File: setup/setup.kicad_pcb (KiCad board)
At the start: 2 copper layers, 54 x 94 mm, 19 parts, among them J1 Conn_01x08_Socket, J11 Motor Power, J2 Conn_01x08_Socket, J3 Step M1, J4 PS2 Controller, J5 Conn_01x22_Socket, J6 Conn_01x22_Socket, J7 6V IN, J8 Additional Outputs, M1 Motor_Servo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

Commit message: feat: add oled(pcb)
Signed-off-by: kyle <kyle@nixos-portable>
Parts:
- added U1: ER_OLEDM0.91_1x-I2C, Connector_JST:JST_XH_S4B-XH-A-1_1x04_P2.50mm_Horizontal, F.Cu at (146.5, 42.0)
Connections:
- J6 pad 4: unconnected-(J6-1-Pad4) -> Net-(J6-1)
- J6 pad 5: unconnected-(J6-2-Pad5) -> Net-(J6-2)
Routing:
- net Net-(J2-VDD): track 135.7 -> 178.3 mm
- net Net-(J6-2): track 0.00 -> 23.5 mm
- net Net-(J6-1): track 0.00 -> 22.0 mm

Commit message: feat: re-order pcb
Signed-off-by: kyle <kyle@nixos-desktop>
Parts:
- removed J8: Additional Outputs, Connector_PinSocket_2.54mm:PinSocket_1x08_P2.54mm_Vertical
- moved M8 54.0 mm to (133.0, 63.6), turned to -90 degrees
- moved M7 51.7 mm to (124.0, 63.6), turned to -90 degrees
- moved M4 27.7 mm to (133.0, 34.5), turned to -90 degrees
- moved M5 27.7 mm to (133.0, 44.0), turned to -90 degrees
- moved M6 27.7 mm to (133.0, 53.5), turned to -90 degrees
- moved C1 19.5 mm to (134.5, 103.0)
- moved U1 11.6 mm to (154.8, 33.9)
- moved J5 10.0 mm to (139.1, 34.2)
- moved J6 10.0 mm to (164.5, 34.2)
- moved J1 9.62 mm to (144.3, 98.5)
- moved J2 9.62 mm to (157.0, 98.5)
- moved J3 8.94 mm to (163.1, 101.0)
- moved J4 7.83 mm to (123.2, 73.8)
- moved J7 6.31 mm to (124.5, 94.0)
- moved J11 6.31 mm to (124.5, 102.5)
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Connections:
- C1 pad 2: Net-(J2-VMOTOR) -> GND
- J2 pad 1: Net-(J2-VMOTOR) -> Net-(J11-12V)
- J4 pad 2: Net-(J4-VCC) -> Net-(J2-VDD)
- J5 pad 21: Net-(J4-VCC) -> Net-(J5-5VIn)
- J6 pad 13: Net-(J6-35) -> unconnected-(J6-35-Pad13)
- J6 pad 14: Net-(J6-0) -> unconnected-(J6-0-Pad14)
- J6 pad 15: Net-(J6-45) -> unconnected-(J6-45-Pad15)
- J6 pad 16: Net-(J6-48) -> unconnected-(J6-48-Pad16)
- J6 pad 17: Net-(J6-47) -> unconnected-(J6-47-Pad17)
- J6 pad 18: Net-(J6-21) -> unconnected-(J6-21-Pad18)
- J6 pad 19: Net-(J6-20) -> unconnected-(J6-20-Pad19)
- J6 pad 20: Net-(J6-19) -> unconnected-(J6-19-Pad20)
- J7 pad 1: Net-(J4-VCC) -> Net-(J5-5VIn)
- M1 pad 2: Net-(J4-VCC) -> Net-(J5-5VIn)
- M2 pad 2: Net-(J4-VCC) -> Net-(J5-5VIn)
- M3 pad 2: Net-(J4-VCC) -> Net-(J5-5VIn)
- M4 pad 2: Net-(J4-VCC) -> Net-(J5-5VIn)
- M5 pad 2: Net-(J4-VCC) -> Net-(J5-5VIn)
- M6 pad 2: Net-(J4-VCC) -> Net-(J5-5VIn)
- M7 pad 2: Net-(J4-VCC) -> Net-(J5-5VIn)
- M8 pad 2: Net-(J4-VCC) -> Net-(J5-5VIn)
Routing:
- net Net-(J4-VCC): track 279.5 -> 0.00 mm
- net Net-(J5-5VIn): track 0.00 -> 124.3 mm
- net Net-(J5-16): track 69.9 -> 6.53 mm
- net Net-(J5-18): track 70.9 -> 7.75 mm
- net Net-(J5-17): track 65.0 -> 17.8 mm
- net Net-(J5-15): track 59.0 -> 12.3 mm
- net Net-(J2-VMOTOR): track 31.3 -> 0.00 mm
- net Net-(M4-PWM): track 49.6 -> 19.1 mm
- net Net-(M3-PWM): track 13.3 -> 42.3 mm
- net Net-(M2-PWM): track 7.59 -> 31.7 mm
- net Net-(J11-12V): track 32.7 -> 54.5 mm
- net Net-(M1-PWM): track 7.29 -> 23.8 mm
- net Net-(J4-DAT): track 7.77 -> 18.3 mm
- net Net-(J1-DIR): track 60.2 -> 50.6 mm
- net Net-(J4-CMD): track 7.99 -> 16.9 mm
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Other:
- outline, holes or cut-outs redrawn
- board text removed: "0"
- board text removed: "19"
- board text removed: "20"
- board text removed: "24"
- board text removed: "36"
- board text removed: "45"
- board text removed: "47"
- board text removed: "48"

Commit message: feat: swap below upper
Signed-off-by: kyle <kyle@nixos-desktop>
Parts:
- moved U1 74.5 mm to (149.8, 108.2), turned to 0 degrees
- moved C1 65.5 mm to (134.0, 37.5)
- moved J1 65.5 mm to (143.8, 33.0)
- moved J11 65.5 mm to (124.0, 37.0)
- moved J2 65.5 mm to (156.5, 33.0)
- moved J3 65.5 mm to (162.6, 35.5)
- moved J7 65.5 mm to (124.0, 28.5)
- moved Jf1 65.5 mm to (124.0, 46.0)
- moved J4 19.2 mm to (124.0, 93.0)
- moved M3 19.2 mm to (124.8, 72.7)
- moved M6 19.2 mm to (133.8, 72.7)
- moved J5 19.2 mm to (139.8, 53.4)
- moved J6 19.2 mm to (165.2, 53.4)
- moved M1 19.2 mm to (124.8, 53.6)
- moved M2 19.2 mm to (124.8, 63.1)
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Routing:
- net Net-(J2-VDD): track 184.8 -> 129.2 mm
- net Net-(J6-1): track 18.1 -> 51.5 mm
- net Net-(J6-2): track 21.6 -> 47.9 mm
- net Net-(J5-5VIn): track 124.3 -> 142.9 mm
- net Net-(J1-DIR): track 50.6 -> 44.1 mm
- net Net-(J1-STEP): track 45.0 -> 49.8 mm
- net Net-(J11-12V): track 54.5 -> 53.2 mm

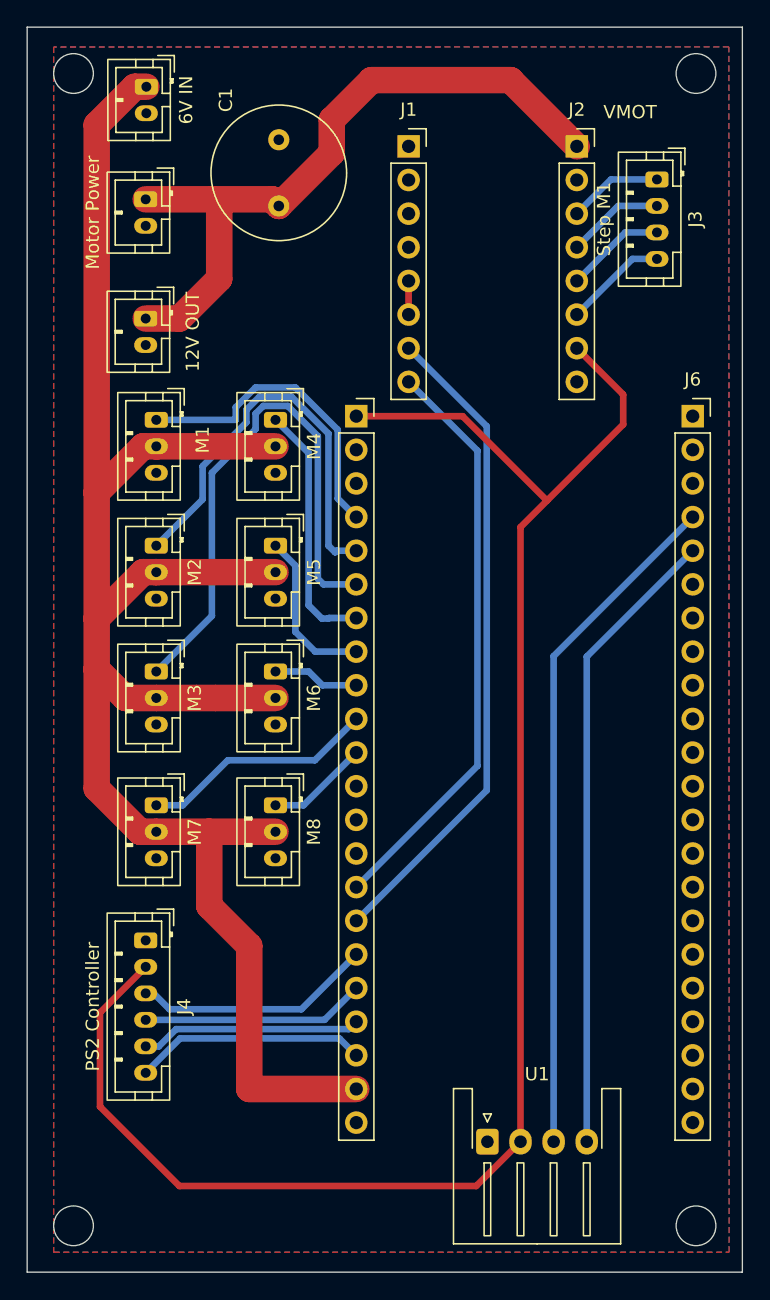
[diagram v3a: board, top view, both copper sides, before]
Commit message: feat: use two-layer routing for motor voltages
Signed-off-by: kyle <kyle@nixos-desktop>
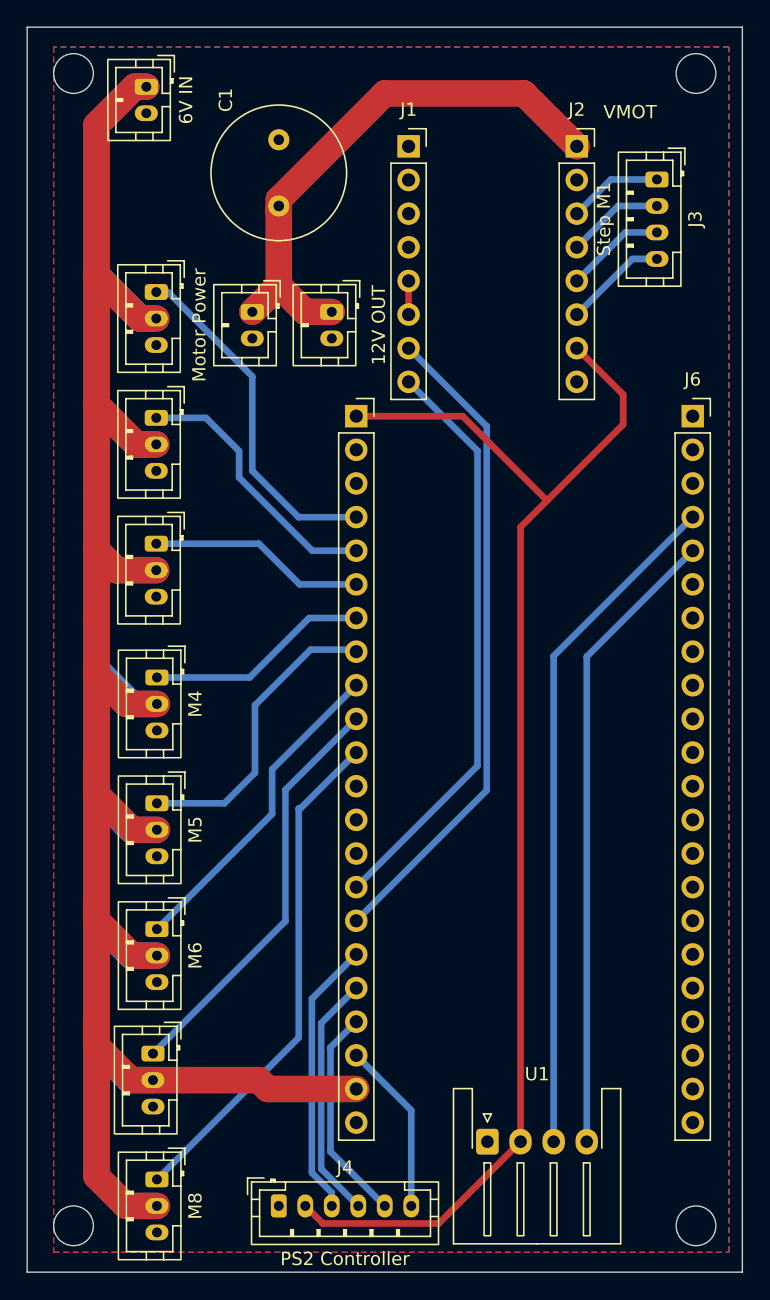
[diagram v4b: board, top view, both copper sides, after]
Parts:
- moved M8 29.6 mm to (124.8, 111.0)
- moved J4 22.4 mm to (134.0, 113.0), turned to 0 degrees
- moved M4 21.4 mm to (124.8, 73.1)
- moved M5 21.4 mm to (124.8, 82.6)
- moved M6 21.4 mm to (124.8, 92.1)
- moved M7 18.8 mm to (124.5, 101.5)
- moved Jf1 14.1 mm to (138.0, 45.5)
- moved J11 11.7 mm to (132.0, 45.5)
- moved M3 9.65 mm to (124.8, 63.0)
- moved M1 9.65 mm to (124.8, 44.0)
- moved M2 9.65 mm to (124.8, 53.5)
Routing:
- net Net-(J5-5VIn): track 142.9 -> 280.2 mm
- net Net-(J5-18): track 7.75 -> 38.5 mm
- net Net-(J2-VDD): track 129.2 -> 101.0 mm
- net Net-(M3-PWM): track 42.3 -> 16.4 mm
- net Net-(J5-16): track 6.53 -> 24.6 mm
- net Net-(J5-17): track 17.8 -> 31.6 mm
- net Net-(M2-PWM): track 31.7 -> 20.4 mm
- net Net-(J11-12V): track 53.2 -> 42.1 mm
- net Net-(J5-15): track 12.3 -> 22.9 mm
- net Net-(J4-CLK): track 17.5 -> 13.1 mm
- net Net-(J4-DAT): track 18.3 -> 21.0 mm
- net Net-(M1-PWM): track 23.8 -> 26.3 mm
- net Net-(M4-PWM): track 19.1 -> 16.9 mm
- net Net-(J4-CMD): track 16.9 -> 18.7 mm

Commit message: feat: attempt to add copper fill for servo vins
Signed-off-by: kyle <kyle@nixos-desktop>
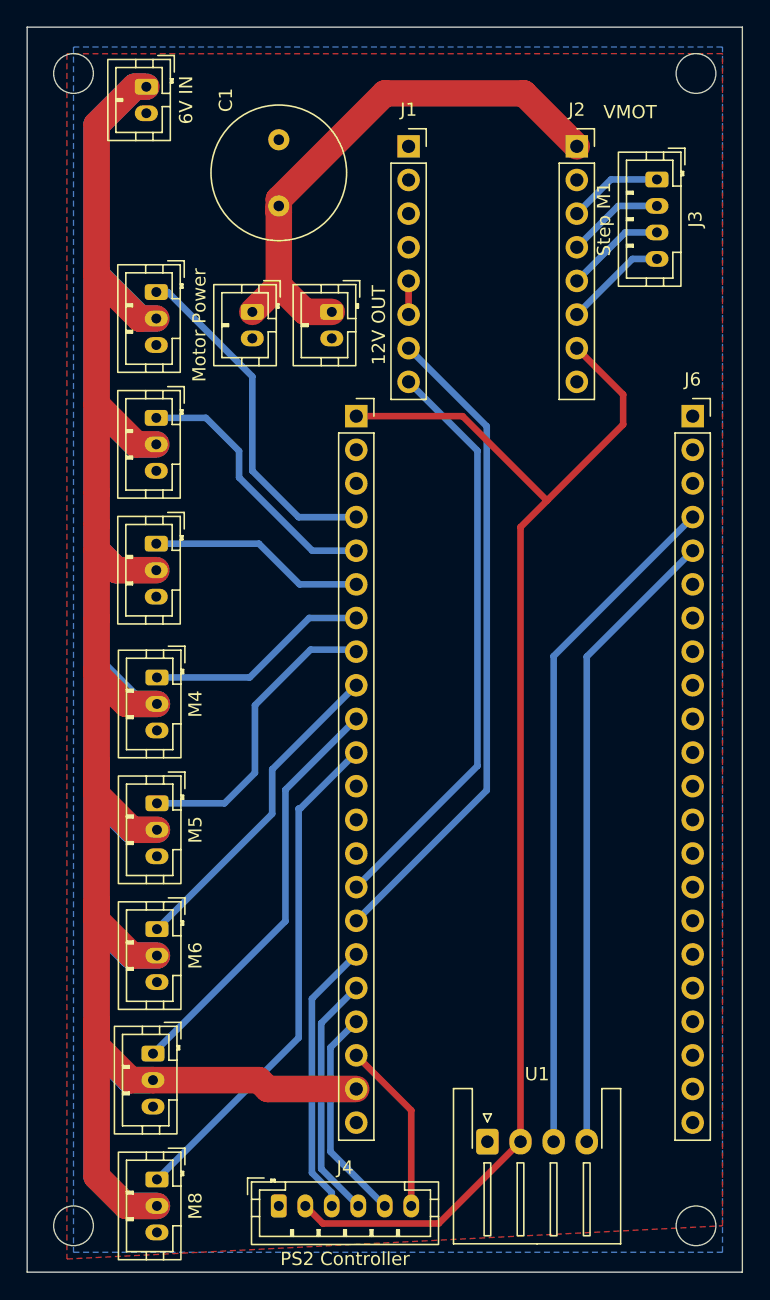
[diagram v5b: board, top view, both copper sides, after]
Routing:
- added copper zone on B.Cu, net Net-(J5-5VIn)
- removed copper zone on B.Cu, net GND
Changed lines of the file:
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@@
 	(segment
 		(start 144 105.78)
-		(end 144 113)
+		(end 139.85 101.63)
 		(width 0.5)
-		(layer "B.Cu")
+		(layer "F.Cu")
 		(net "Net-(J4-CLK)")
 	)
 	(segment
-		(start 139.85 101.63)
+		(start 144 113)
 		(end 144 105.78)
 		(width 0.5)
-		(layer "B.Cu")
+		(layer "F.Cu")
 		(net "Net-(J4-CLK)")
 	)
@@
 	(zone
 		(net "GND")
-		(layers "F.Cu" "B.Cu")
+		(layer "F.Cu")
 		(name "copper fill")
 		(hatch edge 0.5)
@@
 		(polygon
 			(pts
-				(xy 167.98052 25.489088) (xy 117 25.5) (xy 117 116.5) (xy 168 116.5)
+				(xy 167.5 25.999835) (xy 118.000644 26.008026) (xy 118.000644 117.008026) (xy 167.5 114.5)
 			)
 		)
+	)
+	(zone
+		(net "Net-(J5-5VIn)")
+		(layer "B.Cu")
+		(name "copper fill(servos)")
+		(hatch edge 0.5)
+		(connect_pads
+			(clearance 0.5)
+		)
+		(min_thickness 0.25)
+		(fill yes
+			(thermal_gap 0.5)
+			(thermal_bridge_width 0.5)
+			(island_removal_mode 0)
+		)
+		(polygon
+			(pts
+				(xy 167.5 25.5) (xy 118.5 25.5) (xy 118.5 116.5) (xy 167.5 116.5)
+			)
+		)
